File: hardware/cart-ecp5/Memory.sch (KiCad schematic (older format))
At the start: 10 parts, among them J2 MicroSD_Molex_1040310811, U3 S27KS0641

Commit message: Check all resistor values for power management and assign MPN for caps and resistors
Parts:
- C16: MFR (none) -> Samsung; MPN (none) -> CL10A106MQ8NNND
- C17, C69, C70, C71: MFR (none) -> Samsung; MPN (none) -> CL05B104KO5NNNC
- J2: MFR (none) -> Molex
- R1, R8: MFR (none) -> Yageo; MPN (none) -> RC0402FR-0710KL
- RN3: MFR (none) -> Yageo; MPN YC164-JR-0710KL -> YC164-FR-0710KL
- U3: MFR (none) -> Cypress; MPN (none) -> S27KS0641
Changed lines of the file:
@@
 F 2 "ng_package_bga:BGA-24_6.0x8.0mm_Layout5x5_P1.0mm_Pad0.4mm" H 3000 6050 60  0001 C CNN
 F 3 "https://www.cypress.com/file/183506/download" H 3000 6050 60  0001 C CNN
+F 4 "Cypress" H 3800 4100 50  0001 C CNN "MFR"
+F 5 "S27KS0641" H 3800 4100 50  0001 C CNN "MPN"
 	1    3800 4100
 	1    0    0    -1
@@
 F 3 "~" H 8700 4000 50  0001 C CNN
 F 4 "104031-0811" H 8700 4000 50  0001 C CNN "MPN"
+F 5 "Molex" H 8700 4000 50  0001 C CNN "MFR"
 	1    8700 4000
 	1    0    0    -1
@@
 F 2 "Resistor_SMD:R_0402_1005Metric" V 7580 3150 50  0001 C CNN
 F 3 "~" H 7650 3150 50  0001 C CNN
-F 4 "" H 7650 3150 50  0001 C CNN "MPN"
+F 4 "RC0402FR-0710KL" H 7650 3150 50  0001 C CNN "MPN"
+F 5 "Yageo" H 7650 3150 50  0001 C CNN "MFR"
 	1    7650 3150
 	1    0    0    -1
@@
 F 2 "Resistor_SMD:R_Array_Convex_4x0603" V 8275 3150 50  0001 C CNN
 F 3 "~" H 8000 3150 50  0001 C CNN
-F 4 "YC164-JR-0710KL" H 8000 3150 50  0001 C CNN "MPN"
+F 4 "YC164-FR-0710KL" H 8000 3150 50  0001 C CNN "MPN"
+F 5 "Yageo" H 8000 3150 50  0001 C CNN "MFR"
 	1    8000 3150
 	1    0    0    -1
@@
 F 2 "Capacitor_SMD:C_0603_1608Metric" H 6938 2900 50  0001 C CNN
 F 3 "~" H 6900 3050 50  0001 C CNN
-F 4 "" H 6900 3050 50  0001 C CNN "MPN"
+F 4 "CL10A106MQ8NNND" H 6900 3050 50  0001 C CNN "MPN"
+F 5 "Samsung" H 6900 3050 50  0001 C CNN "MFR"
 	1    6900 3050
 	-1   0    0    -1
@@
 F 2 "Capacitor_SMD:C_0402_1005Metric" H 7238 2900 50  0001 C CNN
 F 3 "~" H 7200 3050 50  0001 C CNN
-F 4 "" H 7200 3050 50  0001 C CNN "MPN"
+F 4 "CL05B104KO5NNNC" H 7200 3050 50  0001 C CNN "MPN"
+F 5 "Samsung" H 7200 3050 50  0001 C CNN "MFR"
 	1    7200 3050
 	-1   0    0    -1
@@
 F 2 "Resistor_SMD:R_0402_1005Metric" V 7480 3150 50  0001 C CNN
 F 3 "~" H 7550 3150 50  0001 C CNN
-F 4 "" H 7550 3150 50  0001 C CNN "MPN"
+F 4 "RC0402FR-0710KL" H 7550 3150 50  0001 C CNN "MPN"
+F 5 "Yageo" H 7550 3150 50  0001 C CNN "MFR"
 	1    7550 3150
 	1    0    0    -1
@@
 F 2 "Capacitor_SMD:C_0402_1005Metric" H 3088 2900 50  0001 C CNN
 F 3 "~" H 3050 3050 50  0001 C CNN
+F 4 "Samsung" H 3050 3050 50  0001 C CNN "MFR"
+F 5 "CL05B104KO5NNNC" H 3050 3050 50  0001 C CNN "MPN"
 	1    3050 3050
 	1    0    0    -1
@@
 F 2 "Capacitor_SMD:C_0402_1005Metric" H 2788 2900 50  0001 C CNN
 F 3 "~" H 2750 3050 50  0001 C CNN
+F 4 "Samsung" H 2750 3050 50  0001 C CNN "MFR"
+F 5 "CL05B104KO5NNNC" H 2750 3050 50  0001 C CNN "MPN"
 	1    2750 3050
 	1    0    0    -1
@@
 F 2 "Capacitor_SMD:C_0402_1005Metric" H 2488 2900 50  0001 C CNN
 F 3 "~" H 2450 3050 50  0001 C CNN
+F 4 "Samsung" H 2450 3050 50  0001 C CNN "MFR"
+F 5 "CL05B104KO5NNNC" H 2450 3050 50  0001 C CNN "MPN"
 	1    2450 3050
 	1    0    0    -1

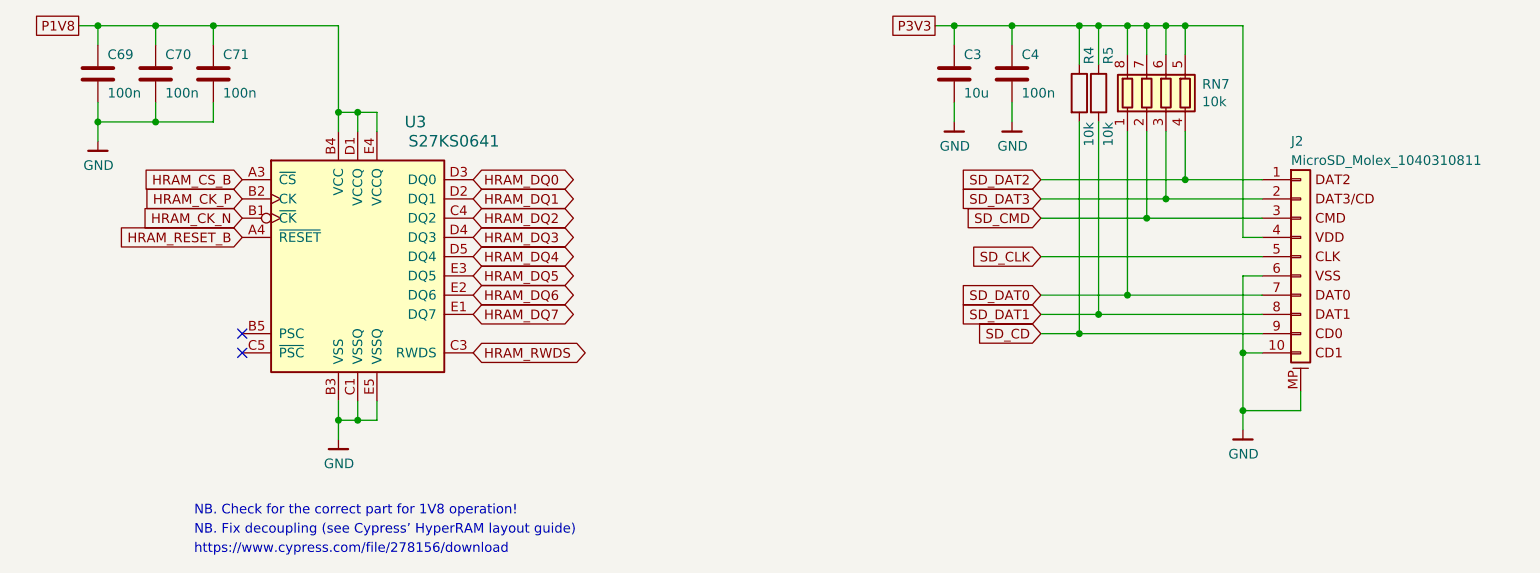
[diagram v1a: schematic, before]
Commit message: Added a copper poor for the sheild of the USB connector
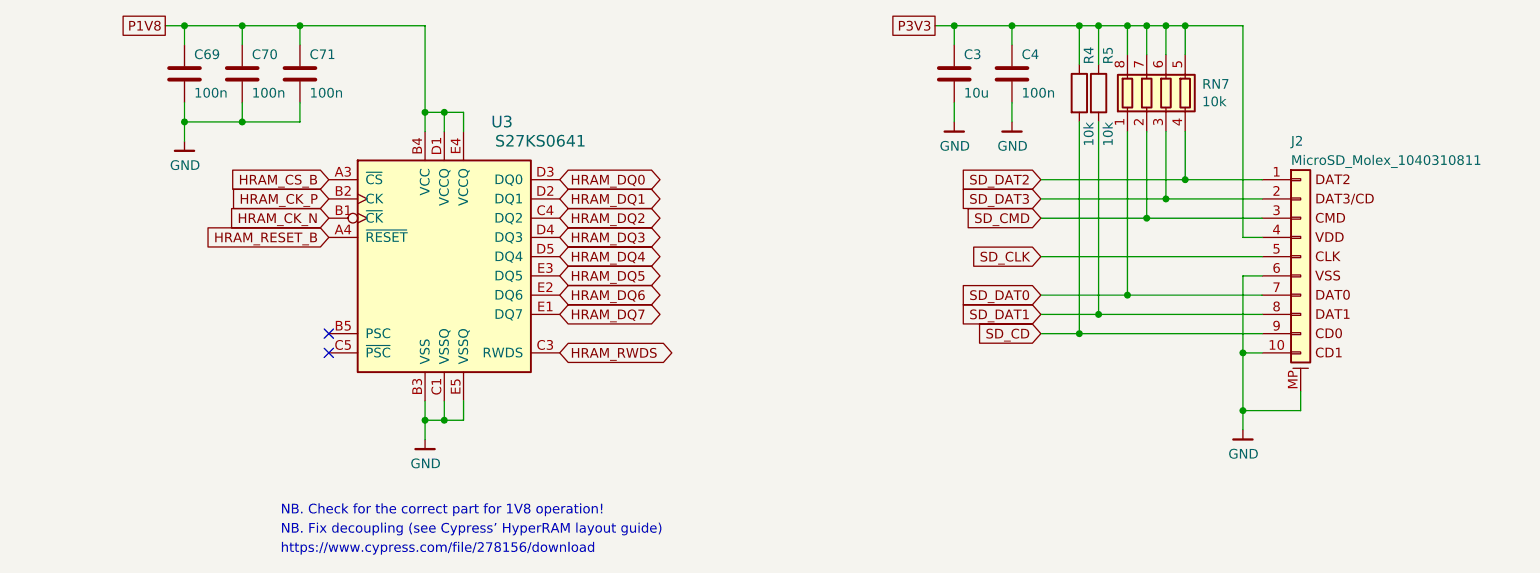
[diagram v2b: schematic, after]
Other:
- moved on the sheet: C69, C70, C71, U3
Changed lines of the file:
@@
 L ng_memory:S27KS0641 U3
 U 1 1 5F47DAAE
-P 3800 4100
-F 0 "U3" H 4100 4900 60  0000 C CNN
-F 1 "S27KS0641" H 4300 4800 60  0000 C CNN
-F 2 "ng_package_bga:BGA-24_6.0x8.0mm_Layout5x5_P1.0mm_Pad0.4mm" H 3000 6050 60  0001 C CNN
-F 3 "https://www.cypress.com/file/183506/download" H 3000 6050 60  0001 C CNN
-F 4 "Cypress" H 3800 4100 50  0001 C CNN "MFR"
-F 5 "S27KS0641" H 3800 4100 50  0001 C CNN "MPN"
-	1    3800 4100
-	1    0    0    -1
-$EndComp
-Text GLabel 4400 3600 2    50   BiDi ~ 0
+P 4250 4100
+F 0 "U3" H 4550 4900 60  0000 C CNN
+F 1 "S27KS0641" H 4750 4800 60  0000 C CNN
+F 2 "ng_package_bga:BGA-24_6.0x8.0mm_Layout5x5_P1.0mm_Pad0.4mm" H 3450 6050 60  0001 C CNN
+F 3 "https://www.cypress.com/file/183506/download" H 3450 6050 60  0001 C CNN
+F 4 "Cypress" H 4250 4100 50  0001 C CNN "MFR"
+F 5 "S27KS0641" H 4250 4100 50  0001 C CNN "MPN"
+	1    4250 4100
+	1    0    0    -1
+$EndComp
+Text GLabel 4850 3600 2    50   BiDi ~ 0
 HRAM_DQ0
-Text GLabel 4400 3700 2    50   BiDi ~ 0
+Text GLabel 4850 3700 2    50   BiDi ~ 0
 HRAM_DQ1
-Text GLabel 4400 3800 2    50   BiDi ~ 0
+Text GLabel 4850 3800 2    50   BiDi ~ 0
 HRAM_DQ2
-Text GLabel 4400 3900 2    50   BiDi ~ 0
+Text GLabel 4850 3900 2    50   BiDi ~ 0
 HRAM_DQ3
-Text GLabel 4400 4000 2    50   BiDi ~ 0
+Text GLabel 4850 4000 2    50   BiDi ~ 0
 HRAM_DQ4
-Text GLabel 4400 4100 2    50   BiDi ~ 0
+Text GLabel 4850 4100 2    50   BiDi ~ 0
 HRAM_DQ5
-Text GLabel 4400 4200 2    50   BiDi ~ 0
+Text GLabel 4850 4200 2    50   BiDi ~ 0
 HRAM_DQ6
-Text GLabel 4400 4300 2    50   BiDi ~ 0
+Text GLabel 4850 4300 2    50   BiDi ~ 0
 HRAM_DQ7
-Text GLabel 4400 4500 2    50   BiDi ~ 0
+Text GLabel 4850 4500 2    50   BiDi ~ 0
 HRAM_RWDS
-NoConn ~ 3200 4400
-NoConn ~ 3200 4500
-Text GLabel 3200 3600 0    50   Input ~ 0
+NoConn ~ 3650 4400
+NoConn ~ 3650 4500
+Text GLabel 3650 3600 0    50   Input ~ 0
 HRAM_CS_B
-Text GLabel 3200 3700 0    50   Input ~ 0
+Text GLabel 3650 3700 0    50   Input ~ 0
 HRAM_CK_P
-Text GLabel 3200 3800 0    50   Input ~ 0
+Text GLabel 3650 3800 0    50   Input ~ 0
 HRAM_CK_N
-Text GLabel 3200 3900 0    50   Input ~ 0
+Text GLabel 3650 3900 0    50   Input ~ 0
 HRAM_RESET_B
 Wire Wire Line
-	3700 3350 3700 3250
-Wire Wire Line
-	3700 3250 3800 3250
-Wire Wire Line
-	3900 3250 3900 3350
-Wire Wire Line
-	3800 3350 3800 3250
-Connection ~ 3800 3250
-Wire Wire Line
-	3800 3250 3900 3250
-Connection ~ 3700 3250
-Text GLabel 2350 2800 0    50   UnSpc ~ 0
+	4150 3350 4150 3250
+Wire Wire Line
+	4150 3250 4250 3250
+Wire Wire Line
+	4350 3250 4350 3350
+Wire Wire Line
+	4250 3350 4250 3250
+Connection ~ 4250 3250
+Wire Wire Line
+	4250 3250 4350 3250
+Connection ~ 4150 3250
+Text GLabel 2800 2800 0    50   UnSpc ~ 0
 P1V8
 Wire Wire Line
-	3700 4750 3700 4850
-Wire Wire Line
-	3700 4850 3800 4850
-Wire Wire Line
-	3800 4850 3800 4750
-Wire Wire Line
-	3800 4850 3900 4850
-Wire Wire Line
-	3900 4850 3900 4750
-Connection ~ 3800 4850
-Wire Wire Line
-	3700 4850 3700 4950
-Connection ~ 3700 4850
+	4150 4750 4150 4850
+Wire Wire Line
+	4150 4850 4250 4850
+Wire Wire Line
+	4250 4850 4250 4750
+Wire Wire Line
+	4250 4850 4350 4850
+Wire Wire Line
+	4350 4850 4350 4750
+Connection ~ 4250 4850
+Wire Wire Line
+	4150 4850 4150 4950
+Connection ~ 4150 4850
 $Comp
 L ng_power:GND #PWR09
 U 1 1 5F3CB04C
-P 3700 4950
-F 0 "#PWR09" H 3700 4700 50  0001 C CNN
-F 1 "GND" H 3703 4824 50  0000 C CNN
-F 2 "" H 3600 4600 50  0001 C CNN
-F 3 "" H 3700 4950 50  0001 C CNN
-	1    3700 4950
+P 4150 4950
+F 0 "#PWR09" H 4150 4700 50  0001 C CNN
+F 1 "GND" H 4153 4824 50  0000 C CNN
+F 2 "" H 4050 4600 50  0001 C CNN
+F 3 "" H 4150 4950 50  0001 C CNN
+	1    4150 4950
 	1    0    0    -1
 $EndComp
@@
 Wire Wire Line
 	8100 3600 8500 3600
-Text Notes 2950 5350 0    50   ~ 0
+Text Notes 3400 5350 0    50   ~ 0
 NB. Check for the correct part for 1V8 operation!
 $Comp
 L Device:C C71
 U 1 1 5F5DCC37
-P 3050 3050
-F 0 "C71" H 3100 3150 50  0000 L CNN
-F 1 "100n" H 3100 2950 50  0000 L CNN
-F 2 "Capacitor_SMD:C_0402_1005Metric" H 3088 2900 50  0001 C CNN
-F 3 "~" H 3050 3050 50  0001 C CNN
-F 4 "Samsung" H 3050 3050 50  0001 C CNN "MFR"
-F 5 "CL05B104KO5NNNC" H 3050 3050 50  0001 C CNN "MPN"
-	1    3050 3050
-	1    0    0    -1
-$EndComp
-Wire Wire Line
-	3050 3200 3050 3300
-Wire Wire Line
-	3050 2900 3050 2800
+P 3500 3050
+F 0 "C71" H 3550 3150 50  0000 L CNN
+F 1 "100n" H 3550 2950 50  0000 L CNN
+F 2 "Capacitor_SMD:C_0402_1005Metric" H 3538 2900 50  0001 C CNN
+F 3 "~" H 3500 3050 50  0001 C CNN
+F 4 "Samsung" H 3500 3050 50  0001 C CNN "MFR"
+F 5 "CL05B104KO5NNNC" H 3500 3050 50  0001 C CNN "MPN"
+	1    3500 3050
+	1    0    0    -1
+$EndComp
+Wire Wire Line
+	3500 3200 3500 3300
+Wire Wire Line
+	3500 2900 3500 2800
 $Comp
 L Device:C C70
 U 1 1 5F5E4A84
-P 2750 3050
-F 0 "C70" H 2800 3150 50  0000 L CNN
-F 1 "100n" H 2800 2950 50  0000 L CNN
-F 2 "Capacitor_SMD:C_0402_1005Metric" H 2788 2900 50  0001 C CNN
-F 3 "~" H 2750 3050 50  0001 C CNN
-F 4 "Samsung" H 2750 3050 50  0001 C CNN "MFR"
-F 5 "CL05B104KO5NNNC" H 2750 3050 50  0001 C CNN "MPN"
-	1    2750 3050
-	1    0    0    -1
-$EndComp
-Wire Wire Line
-	2750 3200 2750 3300
-Wire Wire Line
-	2750 2900 2750 2800
+P 3200 3050
+F 0 "C70" H 3250 3150 50  0000 L CNN
+F 1 "100n" H 3250 2950 50  0000 L CNN
+F 2 "Capacitor_SMD:C_0402_1005Metric" H 3238 2900 50  0001 C CNN
+F 3 "~" H 3200 3050 50  0001 C CNN
+F 4 "Samsung" H 3200 3050 50  0001 C CNN "MFR"
+F 5 "CL05B104KO5NNNC" H 3200 3050 50  0001 C CNN "MPN"
+	1    3200 3050
+	1    0    0    -1
+$EndComp
+Wire Wire Line
+	3200 3200 3200 3300
+Wire Wire Line
+	3200 2900 3200 2800
 $Comp
 L Device:C C69
 U 1 1 5F5E6253
-P 2450 3050
-F 0 "C69" H 2500 3150 50  0000 L CNN
-F 1 "100n" H 2500 2950 50  0000 L CNN
-F 2 "Capacitor_SMD:C_0402_1005Metric" H 2488 2900 50  0001 C CNN
-F 3 "~" H 2450 3050 50  0001 C CNN
-F 4 "Samsung" H 2450 3050 50  0001 C CNN "MFR"
-F 5 "CL05B104KO5NNNC" H 2450 3050 50  0001 C CNN "MPN"
-	1    2450 3050
-	1    0    0    -1
-$EndComp
-Wire Wire Line
-	2450 3200 2450 3300
-Wire Wire Line
-	2450 2900 2450 2800
-Wire Wire Line
-	2450 3300 2750 3300
-Connection ~ 2750 3300
-Wire Wire Line
-	2750 3300 3050 3300
-Wire Wire Line
-	2450 2800 2750 2800
-Wire Wire Line
-	3700 2800 3700 3250
-Connection ~ 2750 2800
-Wire Wire Line
-	2750 2800 3050 2800
-Connection ~ 3050 2800
-Wire Wire Line
-	3050 2800 3700 2800
-Wire Wire Line
-	2450 2800 2350 2800
-Connection ~ 2450 2800
-Wire Wire Line
-	2450 3300 2450 3400
-Connection ~ 2450 3300
+P 2900 3050
+F 0 "C69" H 2950 3150 50  0000 L CNN
+F 1 "100n" H 2950 2950 50  0000 L CNN
+F 2 "Capacitor_SMD:C_0402_1005Metric" H 2938 2900 50  0001 C CNN
+F 3 "~" H 2900 3050 50  0001 C CNN
+F 4 "Samsung" H 2900 3050 50  0001 C CNN "MFR"
+F 5 "CL05B104KO5NNNC" H 2900 3050 50  0001 C CNN "MPN"
+	1    2900 3050
+	1    0    0    -1
+$EndComp
+Wire Wire Line
+	2900 3200 2900 3300
+Wire Wire Line
+	2900 2900 2900 2800
+Wire Wire Line
+	2900 3300 3200 3300
+Connection ~ 3200 3300
+Wire Wire Line
+	3200 3300 3500 3300
+Wire Wire Line
+	2900 2800 3200 2800
+Wire Wire Line
+	4150 2800 4150 3250
+Connection ~ 3200 2800
+Wire Wire Line
+	3200 2800 3500 2800
+Connection ~ 3500 2800
+Wire Wire Line
+	3500 2800 4150 2800
+Wire Wire Line
+	2900 2800 2800 2800
+Connection ~ 2900 2800
+Wire Wire Line
+	2900 3300 2900 3400
+Connection ~ 2900 3300
 $Comp
 L ng_power:GND #PWR068
 U 1 1 5F5F4633
-P 2450 3400
-F 0 "#PWR068" H 2450 3150 50  0001 C CNN
-F 1 "GND" H 2453 3274 50  0000 C CNN
-F 2 "" H 2350 3050 50  0001 C CNN
-F 3 "" H 2450 3400 50  0001 C CNN
-	1    2450 3400
-	1    0    0    -1
-$EndComp
-Text Notes 2950 5450 0    50   ~ 0
+P 2900 3400
+F 0 "#PWR068" H 2900 3150 50  0001 C CNN
+F 1 "GND" H 2903 3274 50  0000 C CNN
+F 2 "" H 2800 3050 50  0001 C CNN
+F 3 "" H 2900 3400 50  0001 C CNN
+	1    2900 3400
+	1    0    0    -1
+$EndComp
+Text Notes 3400 5450 0    50   ~ 0
 NB. Fix decoupling (see Cypress’ HyperRAM layout guide)
-Text Notes 2950 5550 0    50   ~ 0
+Text Notes 3400 5550 0    50   ~ 0
 https://www.cypress.com/file/278156/download
 $EndSCHEMATC

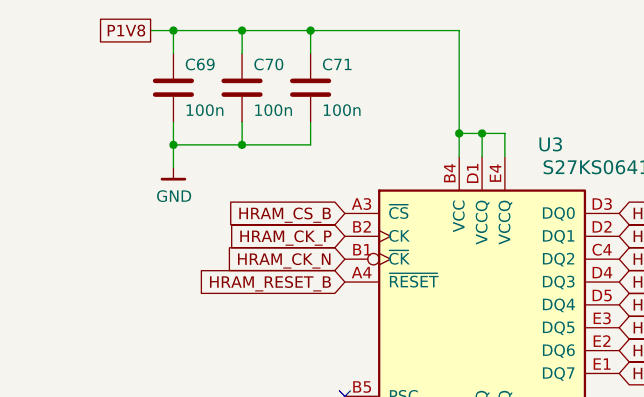
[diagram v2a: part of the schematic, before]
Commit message: Place 1u decoupling caps near hyperram
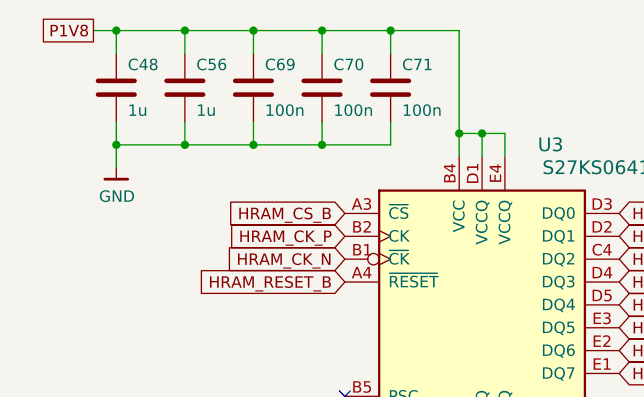
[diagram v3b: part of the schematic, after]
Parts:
- added C48, C56: 1u, Capacitor_SMD:C_0402_1005Metric, symbol Device:C
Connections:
- net GND: now also C48.2, C56.2
- net P1V8: now also C48.1, C56.1
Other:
- moved on the sheet: C69, C70, C71
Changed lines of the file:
@@
 	4250 3250 4350 3250
 Connection ~ 4150 3250
-Text GLabel 2800 2800 0    50   UnSpc ~ 0
+Text GLabel 2550 2800 0    50   UnSpc ~ 0
 P1V8
 Wire Wire Line
@@
 L Device:C C71
 U 1 1 5F5DCC37
-P 3500 3050
-F 0 "C71" H 3550 3150 50  0000 L CNN
-F 1 "100n" H 3550 2950 50  0000 L CNN
-F 2 "Capacitor_SMD:C_0402_1005Metric" H 3538 2900 50  0001 C CNN
-F 3 "~" H 3500 3050 50  0001 C CNN
-F 4 "Samsung" H 3500 3050 50  0001 C CNN "MFR"
-F 5 "CL05B104KO5NNNC" H 3500 3050 50  0001 C CNN "MPN"
-	1    3500 3050
-	1    0    0    -1
-$EndComp
-Wire Wire Line
-	3500 3200 3500 3300
-Wire Wire Line
-	3500 2900 3500 2800
+P 3850 3050
+F 0 "C71" H 3900 3150 50  0000 L CNN
+F 1 "100n" H 3900 2950 50  0000 L CNN
+F 2 "Capacitor_SMD:C_0402_1005Metric" H 3888 2900 50  0001 C CNN
+F 3 "~" H 3850 3050 50  0001 C CNN
+F 4 "Samsung" H 3850 3050 50  0001 C CNN "MFR"
+F 5 "CL05B104KO5NNNC" H 3850 3050 50  0001 C CNN "MPN"
+	1    3850 3050
+	1    0    0    -1
+$EndComp
+Wire Wire Line
+	3850 3200 3850 3300
+Wire Wire Line
+	3850 2900 3850 2800
 $Comp
 L Device:C C70
 U 1 1 5F5E4A84
-P 3200 3050
-F 0 "C70" H 3250 3150 50  0000 L CNN
-F 1 "100n" H 3250 2950 50  0000 L CNN
-F 2 "Capacitor_SMD:C_0402_1005Metric" H 3238 2900 50  0001 C CNN
-F 3 "~" H 3200 3050 50  0001 C CNN
-F 4 "Samsung" H 3200 3050 50  0001 C CNN "MFR"
-F 5 "CL05B104KO5NNNC" H 3200 3050 50  0001 C CNN "MPN"
-	1    3200 3050
-	1    0    0    -1
-$EndComp
-Wire Wire Line
-	3200 3200 3200 3300
-Wire Wire Line
-	3200 2900 3200 2800
+P 3550 3050
+F 0 "C70" H 3600 3150 50  0000 L CNN
+F 1 "100n" H 3600 2950 50  0000 L CNN
+F 2 "Capacitor_SMD:C_0402_1005Metric" H 3588 2900 50  0001 C CNN
+F 3 "~" H 3550 3050 50  0001 C CNN
+F 4 "Samsung" H 3550 3050 50  0001 C CNN "MFR"
+F 5 "CL05B104KO5NNNC" H 3550 3050 50  0001 C CNN "MPN"
+	1    3550 3050
+	1    0    0    -1
+$EndComp
+Wire Wire Line
+	3550 3200 3550 3300
+Wire Wire Line
+	3550 2900 3550 2800
 $Comp
 L Device:C C69
 U 1 1 5F5E6253
-P 2900 3050
-F 0 "C69" H 2950 3150 50  0000 L CNN
-F 1 "100n" H 2950 2950 50  0000 L CNN
-F 2 "Capacitor_SMD:C_0402_1005Metric" H 2938 2900 50  0001 C CNN
-F 3 "~" H 2900 3050 50  0001 C CNN
-F 4 "Samsung" H 2900 3050 50  0001 C CNN "MFR"
-F 5 "CL05B104KO5NNNC" H 2900 3050 50  0001 C CNN "MPN"
-	1    2900 3050
-	1    0    0    -1
-$EndComp
-Wire Wire Line
-	2900 3200 2900 3300
-Wire Wire Line
-	2900 2900 2900 2800
-Wire Wire Line
-	2900 3300 3200 3300
-Connection ~ 3200 3300
-Wire Wire Line
-	3200 3300 3500 3300
-Wire Wire Line
-	2900 2800 3200 2800
+P 3250 3050
+F 0 "C69" H 3300 3150 50  0000 L CNN
+F 1 "100n" H 3300 2950 50  0000 L CNN
+F 2 "Capacitor_SMD:C_0402_1005Metric" H 3288 2900 50  0001 C CNN
+F 3 "~" H 3250 3050 50  0001 C CNN
+F 4 "Samsung" H 3250 3050 50  0001 C CNN "MFR"
+F 5 "CL05B104KO5NNNC" H 3250 3050 50  0001 C CNN "MPN"
+	1    3250 3050
+	1    0    0    -1
+$EndComp
+Wire Wire Line
+	3250 3200 3250 3300
+Wire Wire Line
+	3250 2900 3250 2800
+Wire Wire Line
+	3250 3300 3550 3300
+Connection ~ 3550 3300
+Wire Wire Line
+	3550 3300 3850 3300
+Wire Wire Line
+	3250 2800 3550 2800
 Wire Wire Line
 	4150 2800 4150 3250
-Connection ~ 3200 2800
-Wire Wire Line
-	3200 2800 3500 2800
-Connection ~ 3500 2800
-Wire Wire Line
-	3500 2800 4150 2800
-Wire Wire Line
-	2900 2800 2800 2800
-Connection ~ 2900 2800
-Wire Wire Line
-	2900 3300 2900 3400
-Connection ~ 2900 3300
+Connection ~ 3550 2800
+Wire Wire Line
+	3550 2800 3850 2800
+Wire Wire Line
+	2650 2800 2550 2800
 $Comp
 L ng_power:GND #PWR068
 U 1 1 5F5F4633
-P 2900 3400
-F 0 "#PWR068" H 2900 3150 50  0001 C CNN
-F 1 "GND" H 2903 3274 50  0000 C CNN
-F 2 "" H 2800 3050 50  0001 C CNN
-F 3 "" H 2900 3400 50  0001 C CNN
-	1    2900 3400
+P 2650 3400
+F 0 "#PWR068" H 2650 3150 50  0001 C CNN
+F 1 "GND" H 2653 3274 50  0000 C CNN
+F 2 "" H 2550 3050 50  0001 C CNN
+F 3 "" H 2650 3400 50  0001 C CNN
+	1    2650 3400
 	1    0    0    -1
 $EndComp
@@
 Text Notes 3400 5550 0    50   ~ 0
 https://www.cypress.com/file/278156/download
+$Comp
+L Device:C C56
+U 1 1 6015C35E
+P 2950 3050
+F 0 "C56" H 3000 3150 50  0000 L CNN
+F 1 "1u" H 3000 2950 50  0000 L CNN
+F 2 "Capacitor_SMD:C_0402_1005Metric" H 2988 2900 50  0001 C CNN
+F 3 "~" H 2950 3050 50  0001 C CNN
+F 4 "Samsung" H 2950 3050 50  0001 C CNN "MFR"
+F 5 "CL05A105KO5NNNC" H 2950 3050 50  0001 C CNN "MPN"
+	1    2950 3050
+	1    0    0    -1
+$EndComp
+Wire Wire Line
+	2950 3200 2950 3300
+Wire Wire Line
+	2950 2900 2950 2800
+$Comp
+L Device:C C48
+U 1 1 6015C36C
+P 2650 3050
+F 0 "C48" H 2700 3150 50  0000 L CNN
+F 1 "1u" H 2700 2950 50  0000 L CNN
+F 2 "Capacitor_SMD:C_0402_1005Metric" H 2688 2900 50  0001 C CNN
+F 3 "~" H 2650 3050 50  0001 C CNN
+F 4 "Samsung" H 2650 3050 50  0001 C CNN "MFR"
+F 5 "CL05A105KO5NNNC" H 2650 3050 50  0001 C CNN "MPN"
+	1    2650 3050
+	1    0    0    -1
+$EndComp
+Wire Wire Line
+	2650 2900 2650 2800
+Wire Wire Line
+	2650 3200 2650 3300
+Wire Wire Line
+	2650 3300 2950 3300
+Connection ~ 2650 3300
+Wire Wire Line
+	2650 3300 2650 3400
+Wire Wire Line
+	2950 3300 3250 3300
+Connection ~ 2950 3300
+Connection ~ 3250 3300
+Wire Wire Line
+	2650 2800 2950 2800
+Wire Wire Line
+	2950 2800 3250 2800
+Connection ~ 2950 2800
+Connection ~ 3250 2800
+Connection ~ 2650 2800
+Wire Wire Line
+	3850 2800 4150 2800
+Connection ~ 3850 2800
 $EndSCHEMATC
